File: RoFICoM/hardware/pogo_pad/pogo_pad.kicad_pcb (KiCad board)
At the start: 2 copper layers, 26.5 x 13 mm, 5 parts, among them J1 IN, J2 OUT, J3 POGO

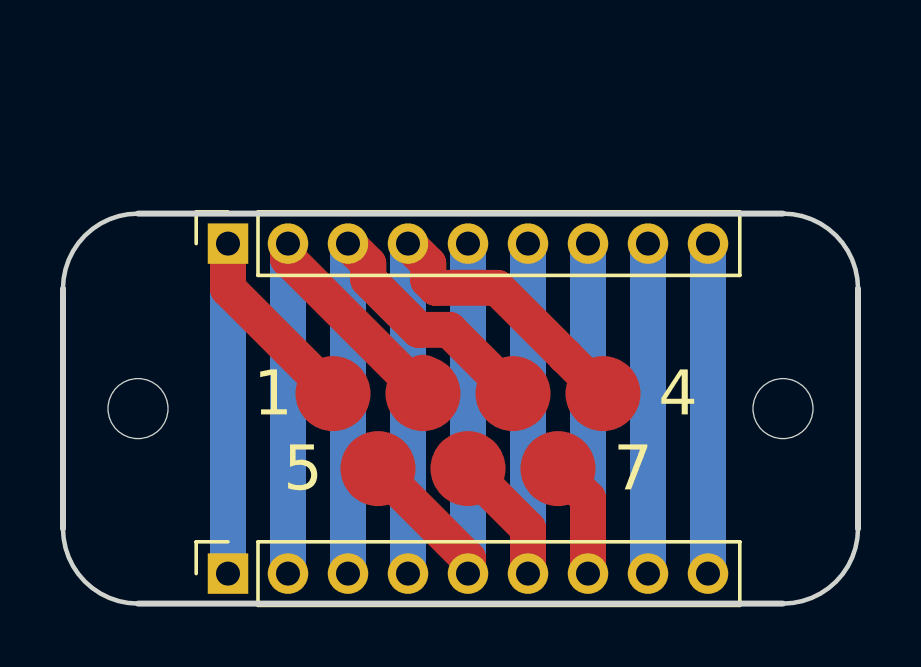
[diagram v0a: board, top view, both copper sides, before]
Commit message: RoFICoM: Add Molex connector to pogo_pad
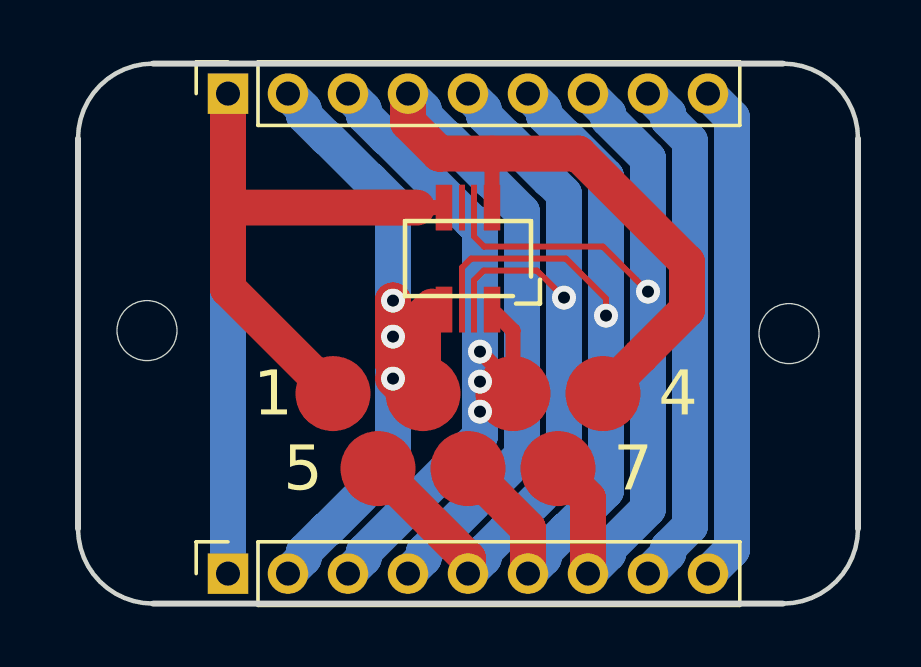
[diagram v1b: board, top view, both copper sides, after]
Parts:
- added J4: Molex, rofi:molex-505004-0812, F.Cu at (118.5, 65.5)
- moved J2 5.00 mm to (110.5, 60.0)
- moved H2 2.62 mm to (107.8, 67.9)
- moved H1 2.51 mm to (129.2, 68.0)
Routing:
- net 4: track 19.9 -> 38.7 mm
- net 1: track 17.4 -> 34.7 mm
- net 6: track 15.6 -> 30.2 mm, vias 0 -> 1
- net 7: track 14.9 -> 29.1 mm, vias 0 -> 1
- net 5: track 15.7 -> 27.9 mm, vias 0 -> 1
- net 2: track 18.7 -> 30.6 mm, vias 0 -> 3
- net 3: track 19.1 -> 27.5 mm, vias 0 -> 3
- net 8: track 11.0 -> 17.2 mm
- net 9: track 11.0 -> 16.7 mm
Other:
- board size 26.5 x 13 mm -> 26 x 18 mm
- board text added: "PogoPads v0.2 9/2019 ro.fi.muni.cz"
- board text removed: "PogoPads v0.1 3/2019 ro.fi.muni.cz"
